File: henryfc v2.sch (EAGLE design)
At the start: 97 parts, among them X1 SM07B-SRSS-TB

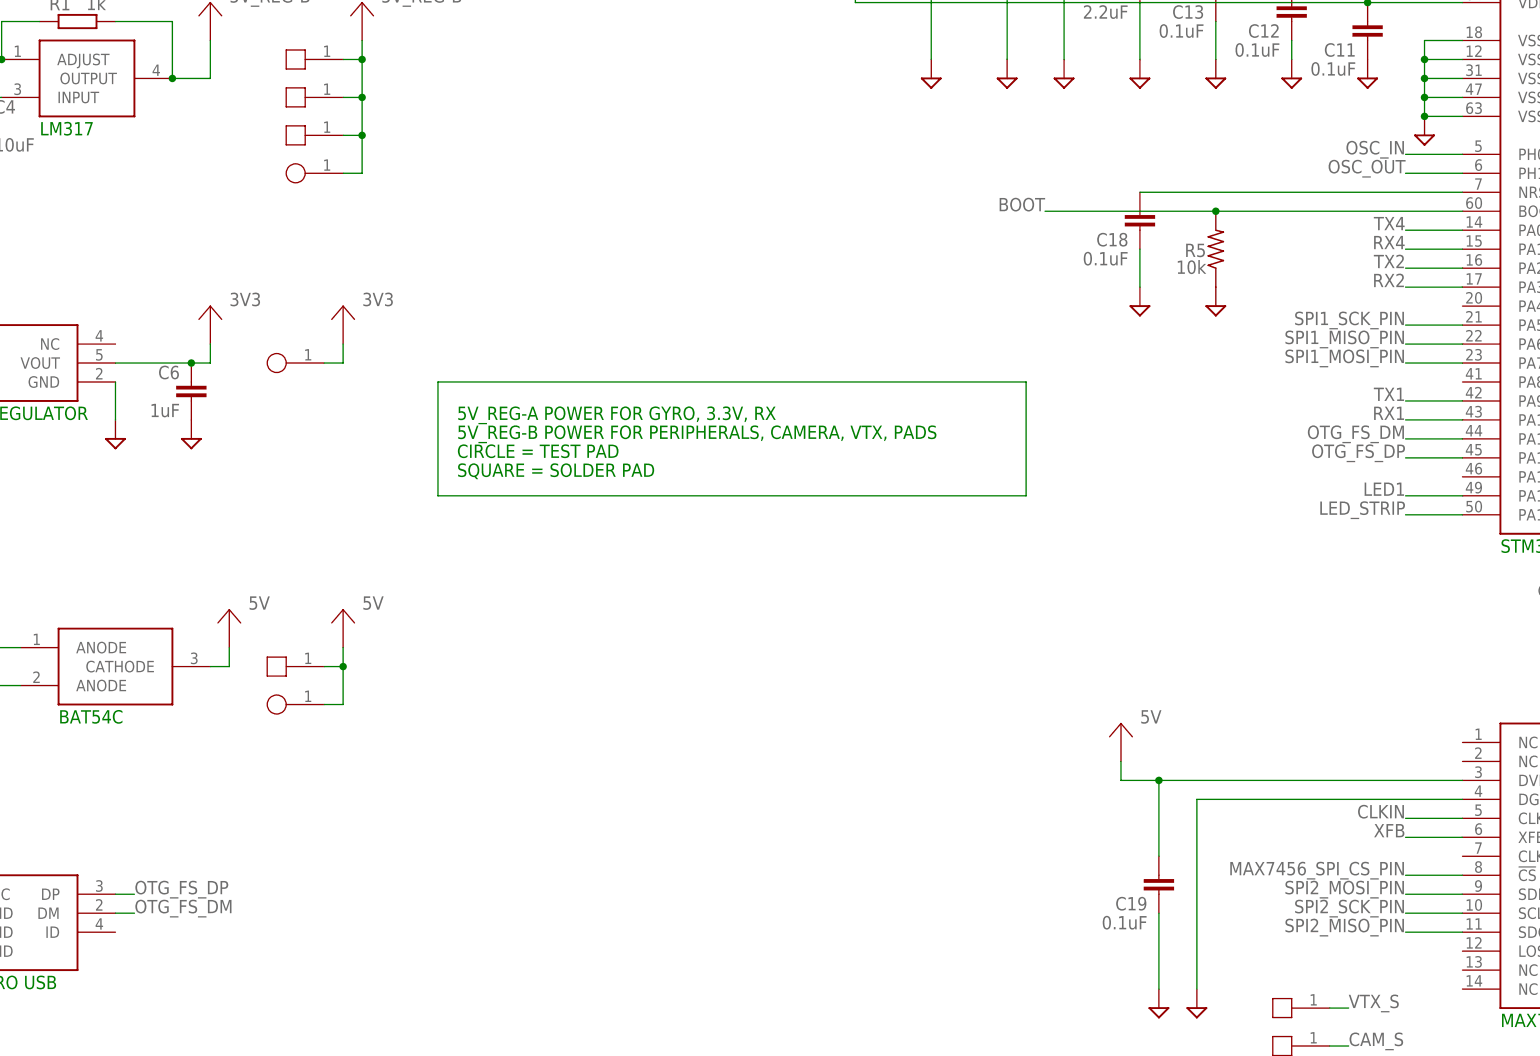
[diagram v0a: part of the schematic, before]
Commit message: updating pcb
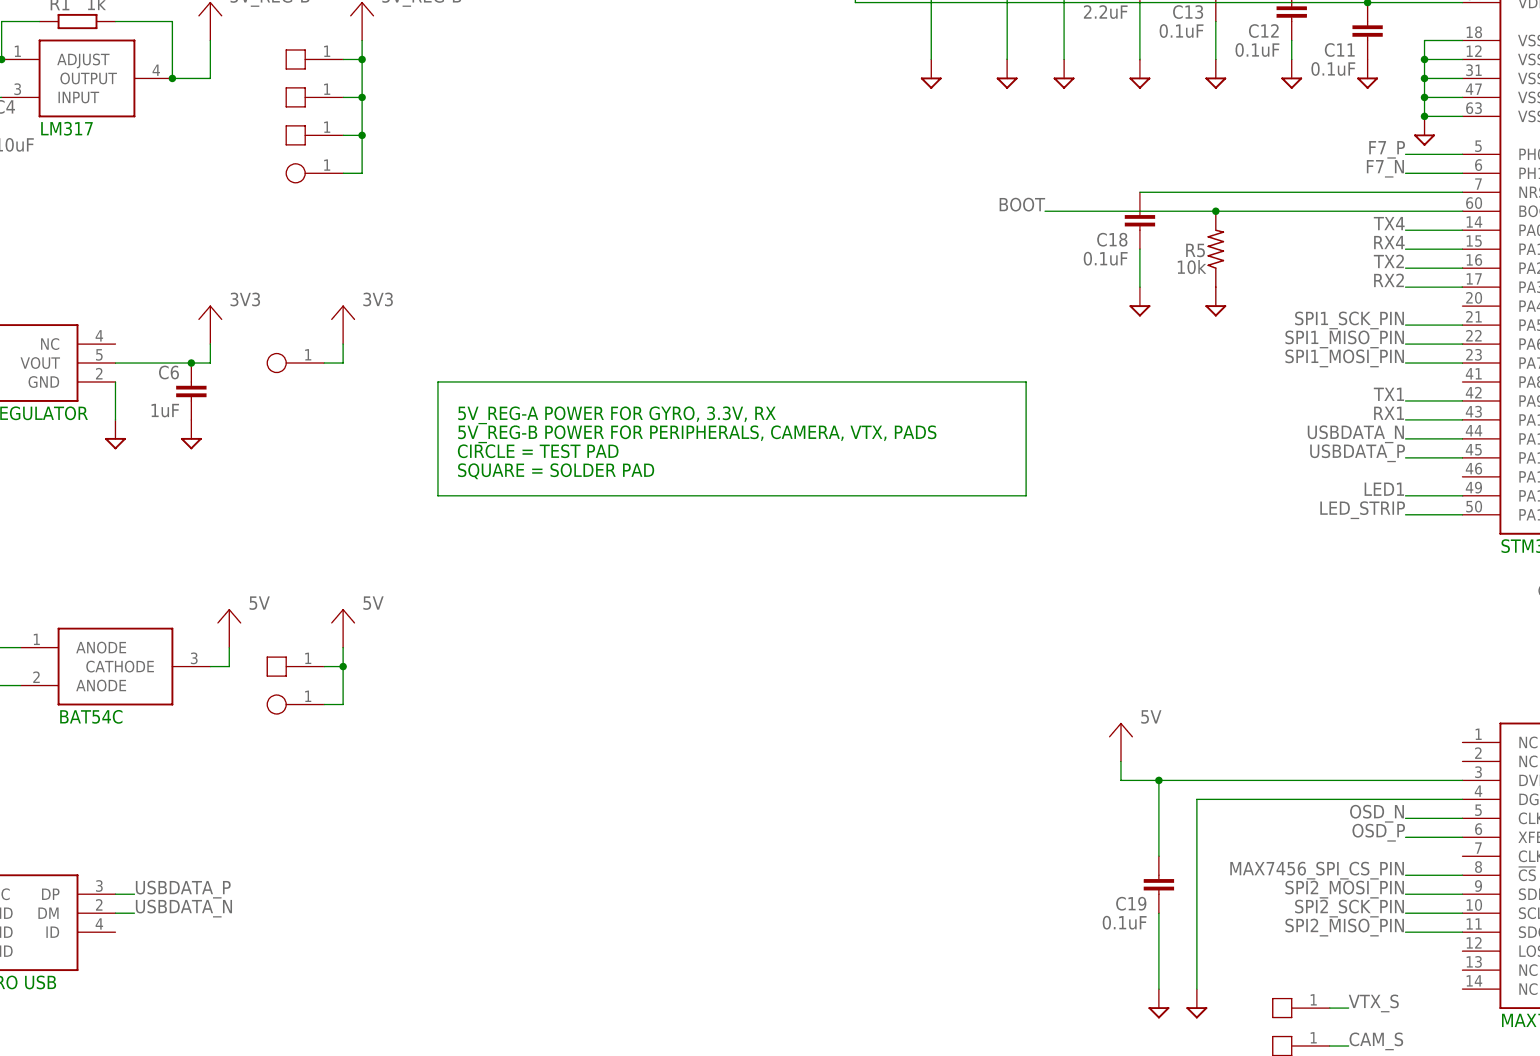
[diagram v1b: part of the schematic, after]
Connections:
- net CLKIN renamed OSD_N
- net OSC_IN renamed F7_P
- net OSC_OUT renamed F7_N
- net OTG_FS_DM renamed USBDATA_N
- net OTG_FS_DP renamed USBDATA_P
- net XFB renamed OSD_P
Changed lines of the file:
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@@
 <part name="SUPPLY35" library="supply2" library_urn="urn:adsk.eagle:library:372" deviceset="GND" device=""/>
 <part name="U$39" library="HenryFC" deviceset="POWER" device=""/>
-<part name="LED1" library="SamacSys_Parts" deviceset="KB_DELPS2.12-QHRI-24-Z555-10-S" device="" override_package3d_urn="urn:adsk.eagle:package:22522683/2" override_package_urn="urn:adsk.eagle:footprint:22522684/1"/>
+<part name="LED1" library="SamacSys_Parts" deviceset="KB_DELPS2.12-QHRI-24-Z555-10-S" device="" override_package3d_urn="urn:adsk.eagle:package:22522683/2" override_package_urn="urn:adsk.eagle:footprint:22522684/1" override_locally_modified="yes"/>
 <part name="LED2" library="SamacSys_Parts" deviceset="KR_DELPS1.22-UHVI-26-H3Q4" device=""/>
 <part name="SUPPLY34" library="supply2" library_urn="urn:adsk.eagle:library:372" deviceset="GND" device=""/>
@@
 </segment>
 </net>
-<net name="OTG_FS_DP" class="0">
+<net name="USBDATA_P" class="0">
 <segment>
 <pinref part="U$6" gate="G$1" pin="DP"/>
@@
 </segment>
 </net>
-<net name="OTG_FS_DM" class="0">
+<net name="USBDATA_N" class="0">
 <segment>
 <pinref part="U$6" gate="G$1" pin="DM"/>
@@
 </segment>
 </net>
-<net name="OSC_IN" class="0">
+<net name="F7_P" class="0">
 <segment>
 <pinref part="U$5" gate="G$1" pin="PH0-OSC_IN"/>
@@
 </segment>
 </net>
-<net name="OSC_OUT" class="0">
+<net name="F7_N" class="0">
 <segment>
 <pinref part="U$5" gate="G$1" pin="PH1-OSC_OUT"/>
@@
 </segment>
 </net>
-<net name="CLKIN" class="0">
+<net name="OSD_N" class="0">
 <segment>
 <pinref part="U$10" gate="G$1" pin="CLKIN"/>
@@
 </segment>
 </net>
-<net name="XFB" class="0">
+<net name="OSD_P" class="0">
 <segment>
 <pinref part="U$10" gate="G$1" pin="XFB"/>
